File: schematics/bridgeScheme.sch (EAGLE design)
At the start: 22 parts

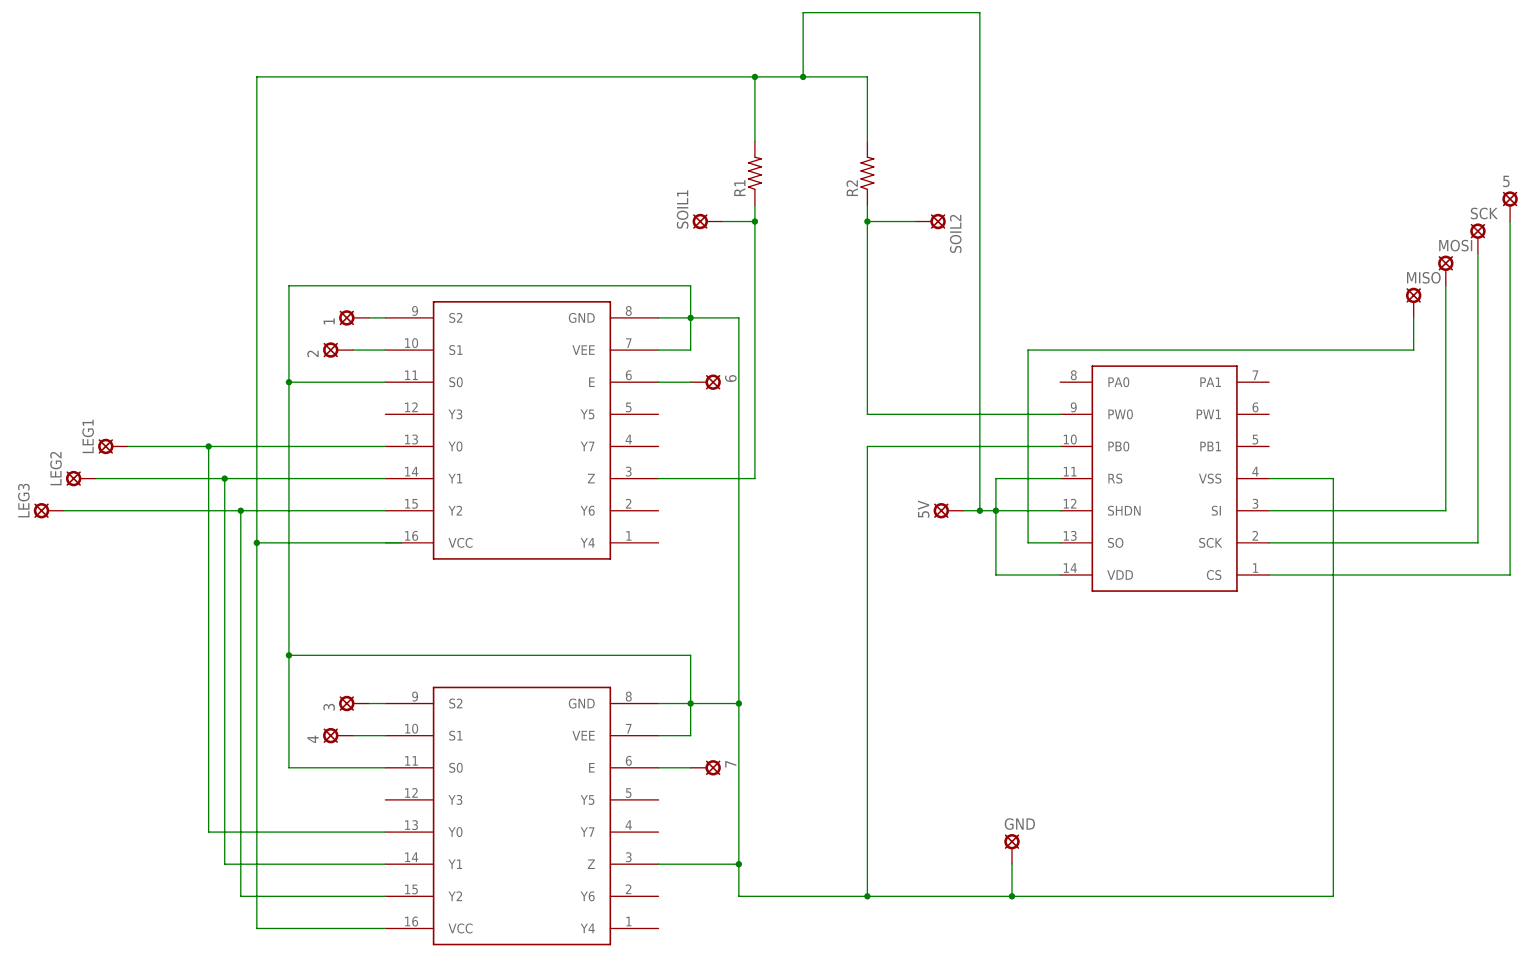
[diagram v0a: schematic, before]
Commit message: Дал имена всем сигналам, исправил две ошибки на плате, утолщил и переразвел некоторые сигналы без переходных отверстий. (Строго говоря всеравно с ними, но они теперь в ножках микросхем)
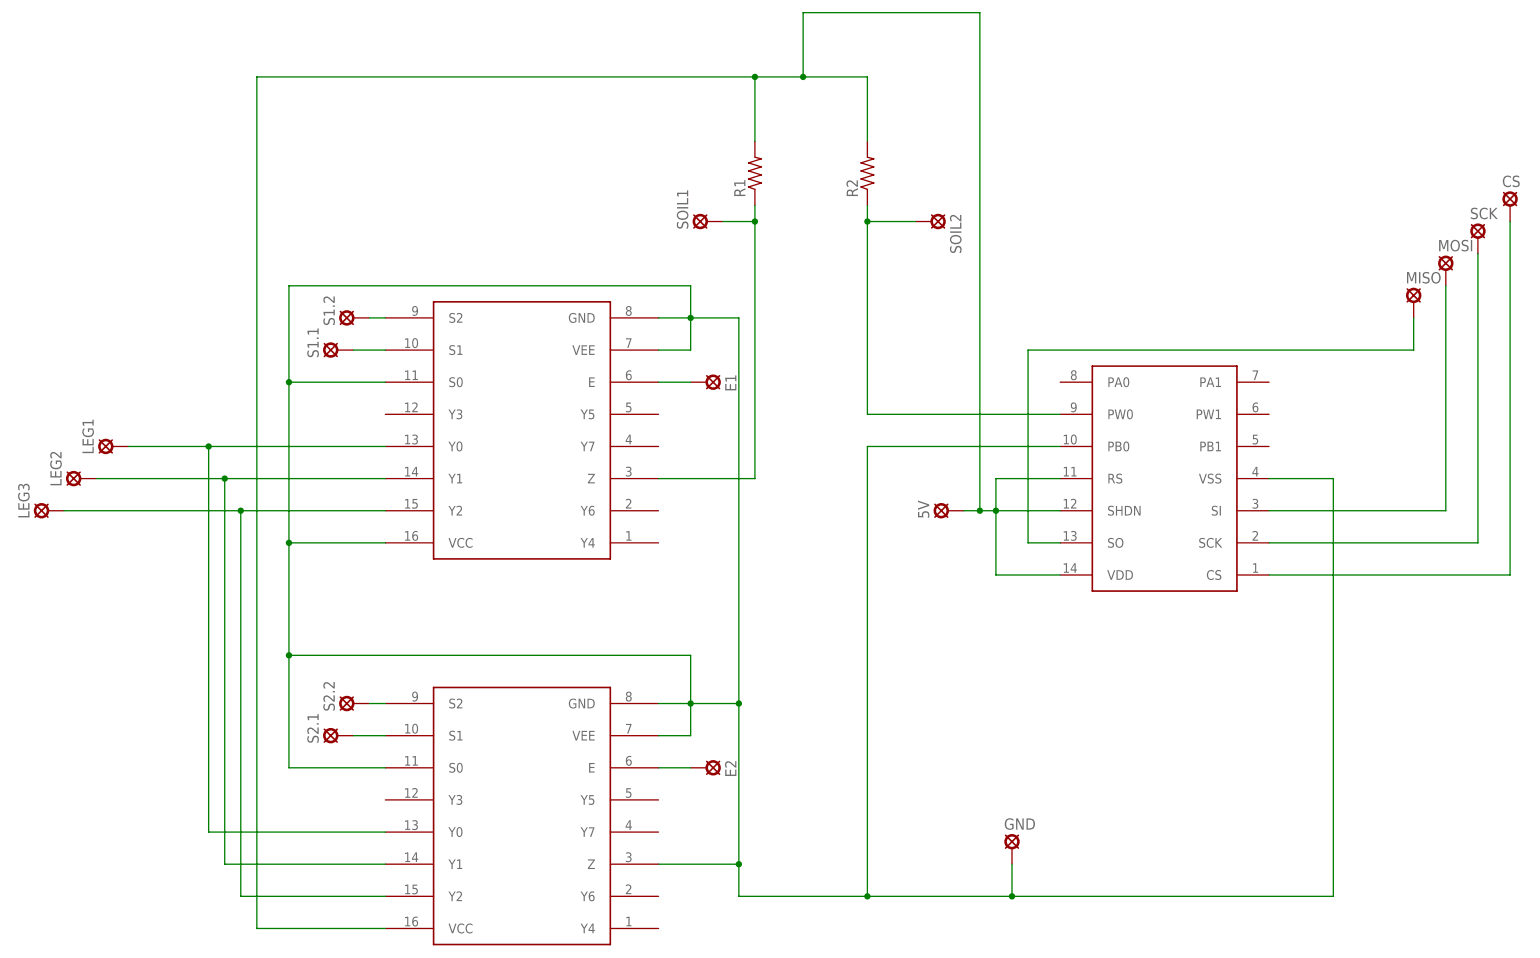
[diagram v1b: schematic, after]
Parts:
- renumbered 1 to S1.2, 2 to S1.1, 3 to S2.2, 4 to S2.1, 5 to CS, 6 to E1, 7 to E2
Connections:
- net N$13 renamed SOIL-1
- net N$15 renamed MISO
- net N$18 renamed CS
- net N$19 renamed SCK
- net N$2 renamed S2.2
- net N$20 renamed MOSI
- net N$3 renamed S2.1
- net N$4 renamed S1.1
- net N$5 renamed S1.2
- net N$6 renamed E1
- net N$7 renamed E2
- removed net N$9: R2.1, SOIL2.MP
- new net SOIL-2: R2.1, SOIL2.MP, U$1.PW0
- net GND: now also U$2.VCC
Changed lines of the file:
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@@
 <?xml version="1.0" encoding="utf-8"?>
 <!DOCTYPE eagle SYSTEM "eagle.dtd">
-<eagle version="7.6.0">
+<eagle version="8.0.2">
 <drawing>
 <settings>
@@
 <part name="LEG3" library="solpad" deviceset="LSP10" device=""/>
 <part name="5V" library="solpad" deviceset="LSP10" device=""/>
-<part name="1" library="solpad" deviceset="LSP10" device=""/>
-<part name="2" library="solpad" deviceset="LSP10" device=""/>
-<part name="3" library="solpad" deviceset="LSP10" device=""/>
-<part name="4" library="solpad" deviceset="LSP10" device=""/>
+<part name="S1.2" library="solpad" deviceset="LSP10" device=""/>
+<part name="S1.1" library="solpad" deviceset="LSP10" device=""/>
+<part name="S2.2" library="solpad" deviceset="LSP10" device=""/>
+<part name="S2.1" library="solpad" deviceset="LSP10" device=""/>
 <part name="SOIL1" library="solpad" deviceset="LSP10" device=""/>
 <part name="SOIL2" library="solpad" deviceset="LSP10" device=""/>
@@
 <part name="MOSI" library="solpad" deviceset="LSP10" device=""/>
 <part name="SCK" library="solpad" deviceset="LSP10" device=""/>
-<part name="5" library="solpad" deviceset="LSP10" device=""/>
-<part name="6" library="solpad" deviceset="LSP10" device=""/>
-<part name="7" library="solpad" deviceset="LSP10" device=""/>
+<part name="CS" library="solpad" deviceset="LSP10" device=""/>
+<part name="E1" library="solpad" deviceset="LSP10" device=""/>
+<part name="E2" library="solpad" deviceset="LSP10" device=""/>
 </parts>
 <sheets>
@@
 <instance part="LEG3" gate="1" x="-116.84" y="-2.54" rot="R90"/>
 <instance part="5V" gate="1" x="25.4" y="-2.54" rot="R90"/>
-<instance part="1" gate="1" x="-68.58" y="27.94" rot="R90"/>
-<instance part="2" gate="1" x="-71.12" y="22.86" rot="R90"/>
-<instance part="3" gate="1" x="-68.58" y="-33.02" rot="R90"/>
-<instance part="4" gate="1" x="-71.12" y="-38.1" rot="R90"/>
+<instance part="S1.2" gate="1" x="-68.58" y="27.94" rot="R90"/>
+<instance part="S1.1" gate="1" x="-71.12" y="22.86" rot="R90"/>
+<instance part="S2.2" gate="1" x="-68.58" y="-33.02" rot="R90"/>
+<instance part="S2.1" gate="1" x="-71.12" y="-38.1" rot="R90"/>
 <instance part="SOIL1" gate="1" x="-12.7" y="43.18" rot="R90"/>
 <instance part="SOIL2" gate="1" x="22.86" y="43.18" rot="R270"/>
@@
 <instance part="MOSI" gate="1" x="104.14" y="35.56"/>
 <instance part="SCK" gate="1" x="109.22" y="40.64"/>
-<instance part="5" gate="1" x="114.3" y="45.72"/>
-<instance part="6" gate="1" x="-12.7" y="17.78" rot="R270"/>
-<instance part="7" gate="1" x="-12.7" y="-43.18" rot="R270"/>
+<instance part="CS" gate="1" x="114.3" y="45.72"/>
+<instance part="E1" gate="1" x="-12.7" y="17.78" rot="R270"/>
+<instance part="E2" gate="1" x="-12.7" y="-43.18" rot="R270"/>
 </instances>
 <busses>
 </busses>
 <nets>
-<net name="N$2" class="0">
+<net name="S2.2" class="0">
 <segment>
 <pinref part="U$3" gate="G$1" pin="S2"/>
 <wire x1="-63.5" y1="-33.02" x2="-66.04" y2="-33.02" width="0.1524" layer="91"/>
-<pinref part="3" gate="1" pin="MP"/>
-</segment>
-</net>
-<net name="N$3" class="0">
+<pinref part="S2.2" gate="1" pin="MP"/>
+</segment>
+</net>
+<net name="S2.1" class="0">
 <segment>
 <pinref part="U$3" gate="G$1" pin="S1"/>
 <wire x1="-63.5" y1="-38.1" x2="-68.58" y2="-38.1" width="0.1524" layer="91"/>
-<pinref part="4" gate="1" pin="MP"/>
-</segment>
-</net>
-<net name="N$4" class="0">
+<pinref part="S2.1" gate="1" pin="MP"/>
+</segment>
+</net>
+<net name="S1.1" class="0">
 <segment>
 <pinref part="U$2" gate="G$1" pin="S1"/>
 <wire x1="-63.5" y1="22.86" x2="-68.58" y2="22.86" width="0.1524" layer="91"/>
-<pinref part="2" gate="1" pin="MP"/>
-</segment>
-</net>
-<net name="N$5" class="0">
+<pinref part="S1.1" gate="1" pin="MP"/>
+</segment>
+</net>
+<net name="S1.2" class="0">
 <segment>
 <pinref part="U$2" gate="G$1" pin="S2"/>
 <wire x1="-63.5" y1="27.94" x2="-66.04" y2="27.94" width="0.1524" layer="91"/>
-<pinref part="1" gate="1" pin="MP"/>
-</segment>
-</net>
-<net name="N$6" class="0">
+<pinref part="S1.2" gate="1" pin="MP"/>
+</segment>
+</net>
+<net name="E1" class="0">
 <segment>
 <pinref part="U$2" gate="G$1" pin="E"/>
 <wire x1="-20.32" y1="17.78" x2="-15.24" y2="17.78" width="0.1524" layer="91"/>
-<pinref part="6" gate="1" pin="MP"/>
-</segment>
-</net>
-<net name="N$7" class="0">
+<pinref part="E1" gate="1" pin="MP"/>
+</segment>
+</net>
+<net name="E2" class="0">
 <segment>
 <pinref part="U$3" gate="G$1" pin="E"/>
 <wire x1="-20.32" y1="-43.18" x2="-15.24" y2="-43.18" width="0.1524" layer="91"/>
-<pinref part="7" gate="1" pin="MP"/>
+<pinref part="E2" gate="1" pin="MP"/>
 </segment>
 </net>
 <net name="5V" class="0">
 <segment>
-<wire x1="-60.96" y1="-7.62" x2="-83.82" y2="-7.62" width="0.1524" layer="91"/>
 <pinref part="U$3" gate="G$1" pin="VCC"/>
 <wire x1="-63.5" y1="-68.58" x2="-83.82" y2="-68.58" width="0.1524" layer="91"/>
-<wire x1="-83.82" y1="-68.58" x2="-83.82" y2="-7.62" width="0.1524" layer="91"/>
-<wire x1="-83.82" y1="-7.62" x2="-83.82" y2="66.04" width="0.1524" layer="91"/>
-<junction x="-83.82" y="-7.62"/>
+<wire x1="-83.82" y1="-68.58" x2="-83.82" y2="66.04" width="0.1524" layer="91"/>
 <wire x1="-83.82" y1="66.04" x2="-5.08" y2="66.04" width="0.1524" layer="91"/>
 <wire x1="-5.08" y1="66.04" x2="-5.08" y2="55.88" width="0.1524" layer="91"/>
@@
 </segment>
 </net>
-<net name="N$13" class="0">
+<net name="SOIL-1" class="0">
 <segment>
 <pinref part="U$2" gate="G$1" pin="Z"/>
@@
 </segment>
 </net>
-<net name="N$9" class="0">
+<net name="SOIL-2" class="0">
 <segment>
 <pinref part="R2" gate="G$1" pin="1"/>
@@
 <wire x1="12.7" y1="43.18" x2="20.32" y2="43.18" width="0.1524" layer="91"/>
 <junction x="12.7" y="43.18"/>
+<pinref part="SOIL2" gate="1" pin="MP"/>
+<pinref part="U$1" gate="G$1" pin="PW0"/>
 <wire x1="12.7" y1="12.7" x2="43.18" y2="12.7" width="0.1524" layer="91"/>
-<pinref part="SOIL2" gate="1" pin="MP"/>
 </segment>
 </net>
@@
 <pinref part="U$3" gate="G$1" pin="S0"/>
 <wire x1="-78.74" y1="-43.18" x2="-63.5" y2="-43.18" width="0.1524" layer="91"/>
-<wire x1="-78.74" y1="17.78" x2="-78.74" y2="-25.4" width="0.1524" layer="91"/>
+<wire x1="-78.74" y1="17.78" x2="-78.74" y2="-7.62" width="0.1524" layer="91"/>
 <junction x="-78.74" y="17.78"/>
 <junction x="-78.74" y="-25.4"/>
+<wire x1="-78.74" y1="-7.62" x2="-78.74" y2="-25.4" width="0.1524" layer="91"/>
 <wire x1="-15.24" y1="-33.02" x2="-7.62" y2="-33.02" width="0.1524" layer="91"/>
 <wire x1="-7.62" y1="-33.02" x2="-7.62" y2="-58.42" width="0.1524" layer="91"/>
@@
 <wire x1="12.7" y1="7.62" x2="12.7" y2="-63.5" width="0.1524" layer="91"/>
 <junction x="12.7" y="-63.5"/>
-</segment>
-</net>
-<net name="N$15" class="0">
+<pinref part="U$2" gate="G$1" pin="VCC"/>
+<wire x1="-63.5" y1="-7.62" x2="-78.74" y2="-7.62" width="0.1524" layer="91"/>
+<junction x="-78.74" y="-7.62"/>
+</segment>
+</net>
+<net name="MISO" class="0">
 <segment>
 <pinref part="U$1" gate="G$1" pin="SO"/>
@@
 </segment>
 </net>
-<net name="N$18" class="0">
+<net name="CS" class="0">
 <segment>
 <pinref part="U$1" gate="G$1" pin="CS"/>
 <wire x1="76.2" y1="-12.7" x2="114.3" y2="-12.7" width="0.1524" layer="91"/>
 <wire x1="114.3" y1="-12.7" x2="114.3" y2="43.18" width="0.1524" layer="91"/>
-<pinref part="5" gate="1" pin="MP"/>
-</segment>
-</net>
-<net name="N$19" class="0">
+<pinref part="CS" gate="1" pin="MP"/>
+</segment>
+</net>
+<net name="SCK" class="0">
 <segment>
 <pinref part="U$1" gate="G$1" pin="SCK"/>
@@
 </segment>
 </net>
-<net name="N$20" class="0">
+<net name="MOSI" class="0">
 <segment>
 <pinref part="U$1" gate="G$1" pin="SI"/>
